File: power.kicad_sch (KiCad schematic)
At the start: 169 parts, among them Q10 SI7613DN-T1-GE3, Q2 BC817-25W, Q3 DZDH0401DW, Q4 DZDH0401DW, Q5 SI7613DN-T1-GE3, Q6 SI7613DN-T1-GE3, Q8 BC817-25W, U1 LT8350RV#PBF, U10 LM3881MME_NOPB, U11 AP22615A_TSOT26, U2 MP2386GG, U3 TPS65983BAZBHR, U9 LM1117MP-3.3_NOPB

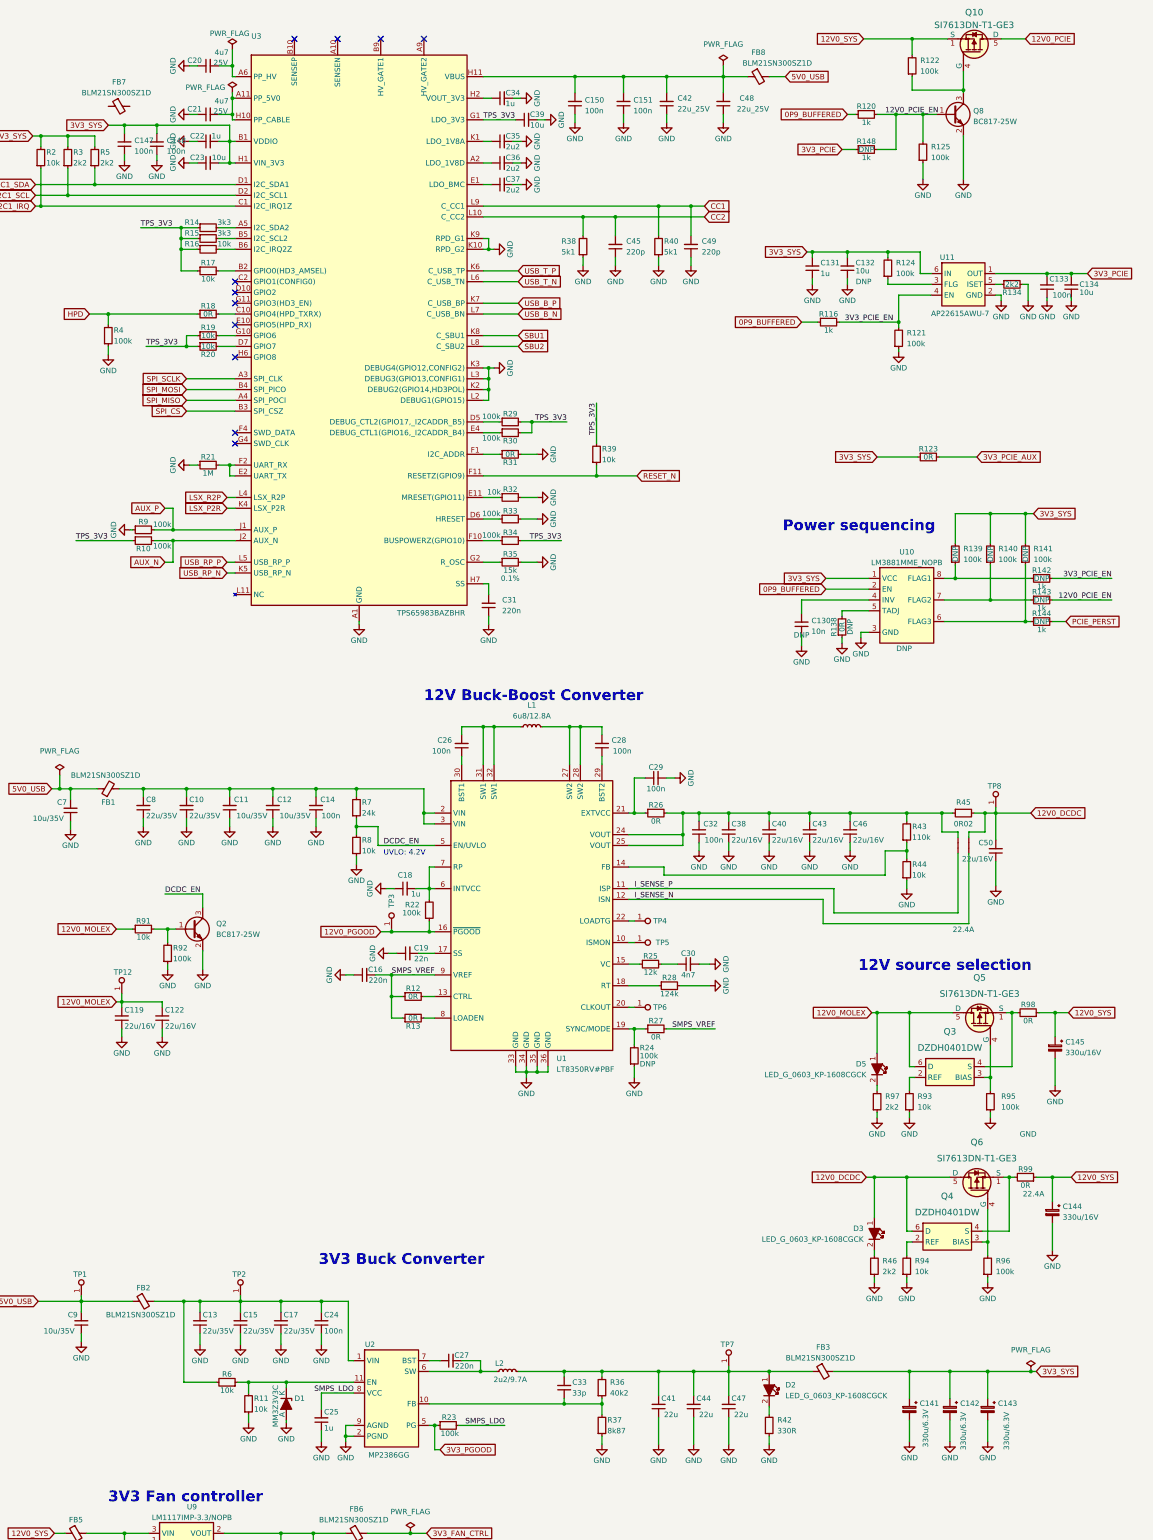
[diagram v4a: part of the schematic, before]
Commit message: Added DNP capacitors in empty spaces
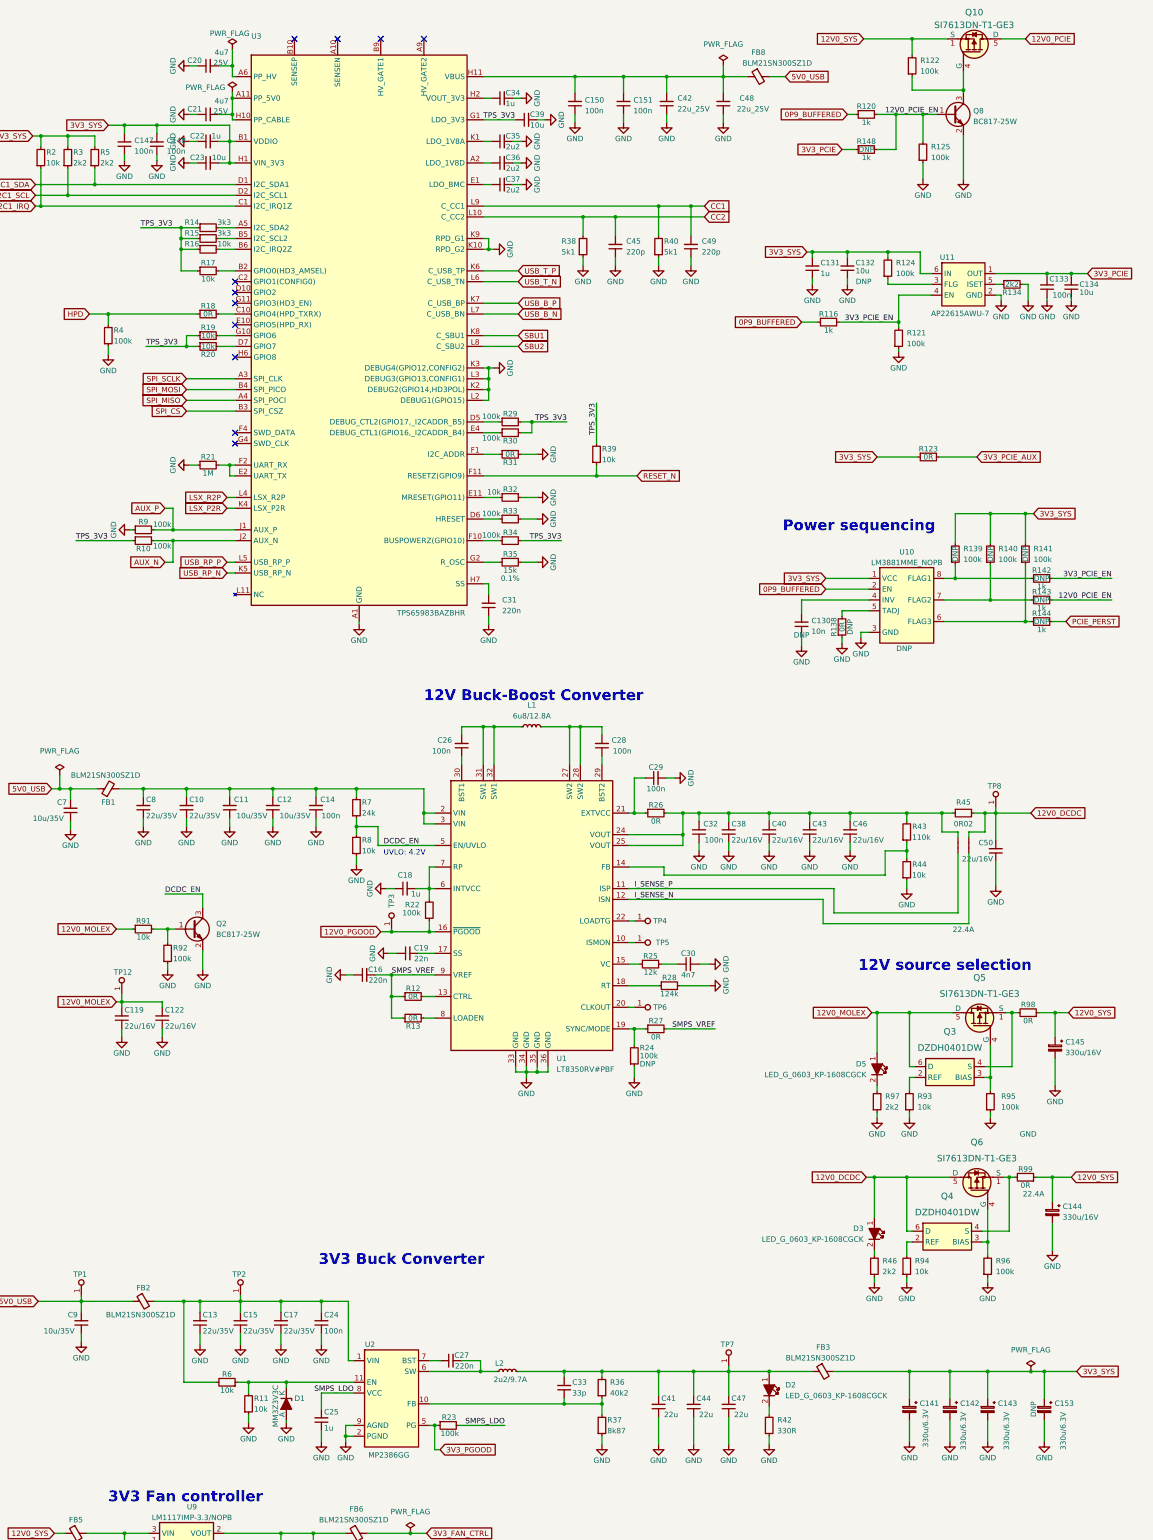
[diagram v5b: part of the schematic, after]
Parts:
- removed FB7: BLM21SN300SZ1D, thunderbolt-gpu-adapter-footprints:FB_0805_2012Metric, symbol thunderbolt-gpu-adapter:BLM21SN300SZ1D
- added C153: C_Pol_330u_6.3V_KEMET-T520-B, antmicro-footprints:C_Pol_EIA-B, symbol antmicroCapacitorspol:C_Pol_330u_6.3V_KEMET-T520-B
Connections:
- net 3V3_SYS: now also C153.1
- net GND: now also C153.2
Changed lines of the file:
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@@
   (junction (at 189.23 215.265) (diameter 0) (color 0 0 0 0)
   )
+  (junction (at 263.525 346.71) (diameter 0) (color 0 0 0 0)
+  )
   (junction (at 71.755 209.55) (diameter 0) (color 0 0 0 0)
   )
@@
     (stroke (width 0) (type default) (color 0 0 0 0))
   )
+  (wire (pts (xy 263.525 346.71) (xy 271.145 346.71))
+    (stroke (width 0) (type default) (color 0 0 0 0))
+  )
   (wire (pts (xy 45.085 242.57) (xy 48.895 242.57))
     (stroke (width 0) (type default) (color 0 0 0 0))
@@
     (stroke (width 0) (type default) (color 0 0 0 0))
   )
+  (wire (pts (xy 263.525 346.71) (xy 263.525 353.06))
+    (stroke (width 0) (type default) (color 0 0 0 0))
+  )
   (wire (pts (xy 51.435 216.535) (xy 51.435 218.44))
     (stroke (width 0) (type default) (color 0 0 0 0))
@@
     (stroke (width 0) (type default) (color 0 0 0 0))
   )
+  (wire (pts (xy 263.525 358.14) (xy 263.525 363.22))
+    (stroke (width 0) (type default) (color 0 0 0 0))
+  )
   (wire (pts (xy 46.355 259.715) (xy 55.88 259.715))
     (stroke (width 0) (type default) (color 0 0 0 0))
@@
     (stroke (width 0) (type default) (color 0 0 0 0))
   )
-  (wire (pts (xy 260.35 346.71) (xy 261.62 346.71))
+  (wire (pts (xy 260.35 346.71) (xy 263.525 346.71))
     (stroke (width 0) (type default) (color 0 0 0 0))
   )
@@
     )
   )
-  (global_label "3V3_SYS" (shape input) (at 261.62 346.71 0) (fields_autoplaced)
+  (global_label "3V3_SYS" (shape input) (at 271.145 346.71 0) (fields_autoplaced)
     (effects (font (size 1.27 1.27)) (justify left))
-    (property "Intersheet References" "${INTERSHEET_REFS}" (id 0) (at 272.016 346.6306 0)
+    (property "Intersheet References" "${INTERSHEET_REFS}" (id 0) (at 281.541 346.6306 0)
       (effects (font (size 1.27 1.27)) (justify left) hide)
     )
@@
     (pin "2")
   )
+  (symbol (lib_id "thunderbolt-gpu-adapter:GND") (at 263.525 363.22 0) (unit 1)
+    (in_bom yes) (on_board yes)
+    (property "Reference" "#PWR0226" (id 0) (at 263.525 369.57 0)
+      (effects (font (size 1.27 1.27)) hide)
+    )
+    (property "Value" "GND" (id 1) (at 263.525 367.03 0))
+    (property "Footprint" "" (id 2) (at 263.525 363.22 0)
+      (effects (font (size 1.27 1.27)) hide)
+    )
+    (property "Datasheet" "" (id 3) (at 263.525 363.22 0)
+      (effects (font (size 1.27 1.27)) hide)
+    )
+    (property "Author" "Antmicro" (id 4) (at 272.415 370.84 0)
+      (effects (font (size 1.27 1.27) (thickness 0.15)) (justify left bottom) hide)
+    )
+    (property "License" "Apache-2.0" (id 5) (at 272.415 373.38 0)
+      (effects (font (size 1.27 1.27) (thickness 0.15)) (justify left bottom) hide)
+    )
+    (pin "1")
+  )
   (symbol (lib_id "thunderbolt-gpu-adapter:C_10n_0402") (at 206.375 173.355 90) (unit 1)
     (in_bom yes) (on_board yes) (fields_autoplaced)
@@
     (pin "2")
   )
+  (symbol (lib_id "antmicroCapacitorspol:C_Pol_330u_6.3V_KEMET-T520-B") (at 263.525 353.06 270) (unit 1)
+    (in_bom yes) (on_board yes)
+    (property "Reference" "C153" (id 0) (at 265.938 354.236 90)
+      (effects (font (size 1.27 1.27) (thickness 0.15)) (justify left))
+    )
+    (property "Value" "C_Pol_330u_6.3V_KEMET-T520-B" (id 1) (at 260.985 367.03 0)
+      (effects (font (size 1.27 1.27) (thickness 0.15)) (justify left bottom) hide)
+    )
+    (property "Footprint" "antmicro-footprints:C_Pol_EIA-B" (id 2) (at 255.905 367.03 0)
+      (effects (font (size 1.27 1.27) (thickness 0.15)) (justify left bottom) hide)
+    )
+    (property "Datasheet" "https://content.kemet.com/datasheets/KEM_T2076_T52X-530.pdf" (id 3) (at 253.365 367.03 0)
+      (effects (font (size 1.27 1.27) (thickness 0.15)) (justify left bottom) hide)
+    )
+    (property "Val" "330u/6.3V" (id 4) (at 267.97 356.235 0)
+      (effects (font (size 1.27 1.27) (thickness 0.15)) (justify left))
+    )
+    (property "MPN" "T520B337M006ATE040" (id 5) (at 250.825 367.03 0)
+      (effects (font (size 1.27 1.27) (thickness 0.15)) (justify left bottom) hide)
+    )
+    (property "Manufacturer" "KEMET" (id 6) (at 248.285 367.03 0)
+      (effects (font (size 1.27 1.27) (thickness 0.15)) (justify left bottom) hide)
+    )
+    (property "License" "Apache-2.0" (id 7) (at 245.745 367.03 0)
+      (effects (font (size 1.27 1.27) (thickness 0.15)) (justify left bottom) hide)
+    )
+    (property "Author" "Antmicro" (id 8) (at 243.205 367.03 0)
+      (effects (font (size 1.27 1.27) (thickness 0.15)) (justify left bottom) hide)
+    )
+    (property "Voltage" "6.3V" (id 9) (at 240.665 367.03 0)
+      (effects (font (size 1.27 1.27)) (justify left bottom) hide)
+    )
+    (property "Dielectric" "template_dielectric" (id 10) (at 238.125 367.03 0)
+      (effects (font (size 1.27 1.27)) (justify left bottom) hide)
+    )
+    (property "DNP" "DNP" (id 11) (at 260.985 355.6 0))
+    (pin "1")
+    (pin "2")
+  )
   (symbol (lib_id "thunderbolt-gpu-adapter:R_8k87_0402") (at 159.385 361.95 90) (unit 1)
     (in_bom yes) (on_board yes)
@@
       (effects (font (size 1.27 1.27) (thickness 0.15)) (justify left bottom) hide)
     )
-    (pin "1")
-    (pin "2")
-  )
-  (symbol (lib_id "thunderbolt-gpu-adapter:BLM21SN300SZ1D") (at 43.18 48.895 0) (mirror x) (unit 1)
-    (in_bom yes) (on_board yes)
-    (property "Reference" "FB7" (id 0) (at 45.72 43.18 0)
-      (effects (font (size 1.27 1.27) (thickness 0.15)))
-    )
-    (property "Value" "BLM21SN300SZ1D" (id 1) (at 45.085 45.72 0)
-      (effects (font (size 1.27 1.27) (thickness 0.15)))
-    )
-    (property "Footprint" "thunderbolt-gpu-adapter-footprints:FB_0805_2012Metric" (id 2) (at 57.15 43.815 0)
-      (effects (font (size 1.27 1.27) (thickness 0.15)) (justify left bottom) hide)
-    )
-    (property "Datasheet" "https://www.murata.com/en-sg/products/productdata/8796738977822/ENFA0005.pdf?1519270210000" (id 3) (at 57.15 41.275 0)
-      (effects (font (size 1.27 1.27) (thickness 0.15)) (justify left bottom) hide)
-    )
-    (property "MPN" "BLM21SN300SZ1D" (id 4) (at 57.15 38.735 0)
-      (effects (font (size 1.27 1.27) (thickness 0.15)) (justify left bottom) hide)
-    )
-    (property "Manufacturer" "Murata" (id 5) (at 57.15 36.195 0)
-      (effects (font (size 1.27 1.27) (thickness 0.15)) (justify left bottom) hide)
-    )
-    (property "License" "Apache-2.0" (id 7) (at 57.15 31.115 0)
-      (effects (font (size 1.27 1.27) (thickness 0.15)) (justify left bottom) hide)
-    )
-    (property "Author" "Antmicro" (id 8) (at 57.15 33.655 0)
-      (effects (font (size 1.27 1.27) (thickness 0.15)) (justify left bottom) hide)
-    )

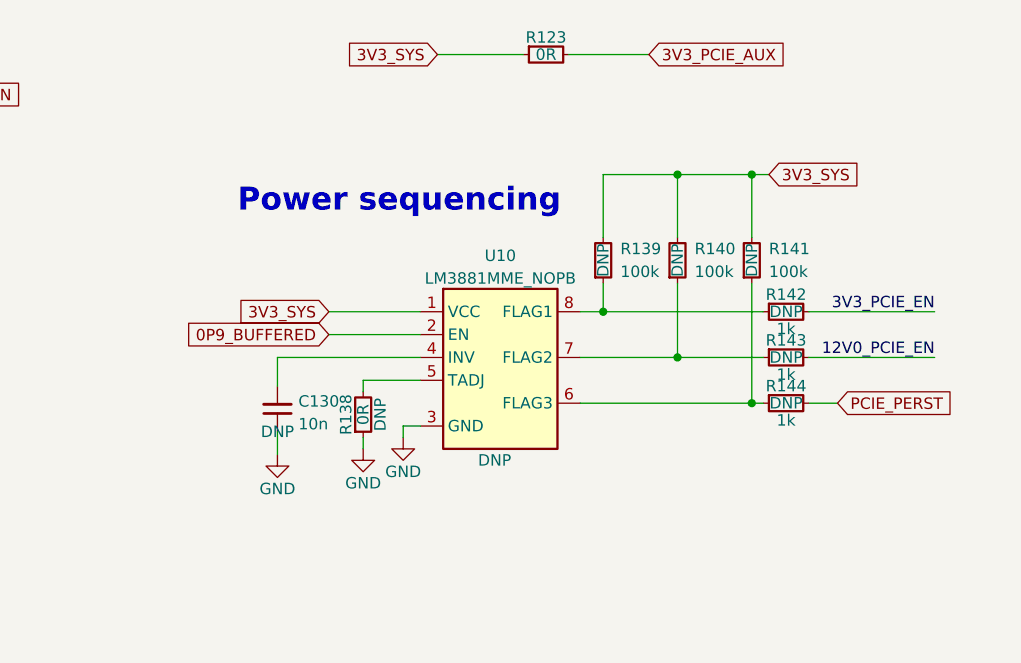
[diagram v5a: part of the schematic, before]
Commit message: Removed optional power sequencing
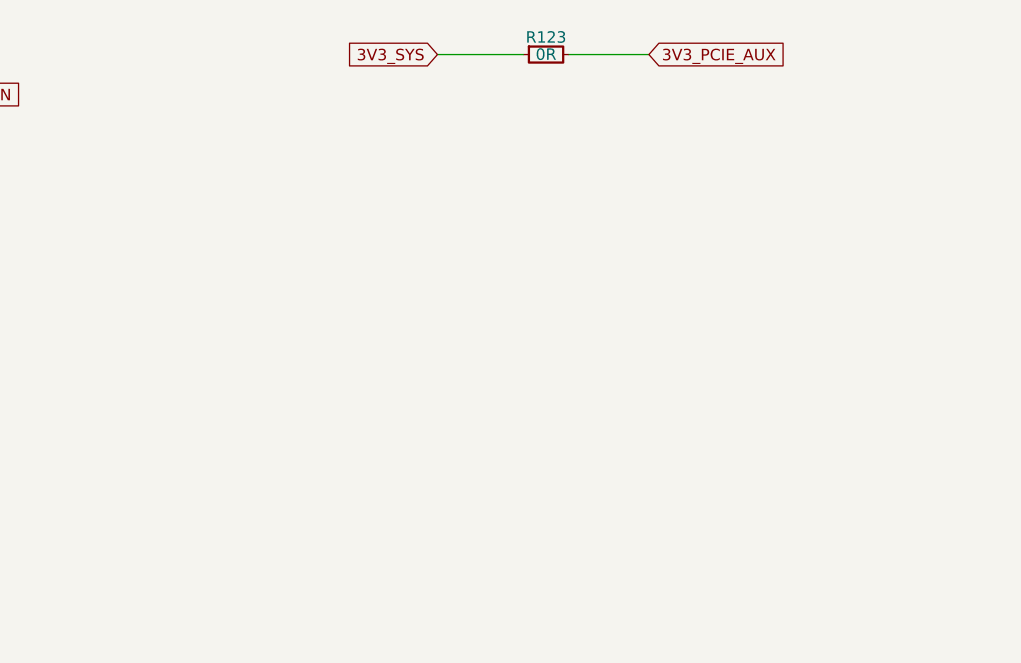
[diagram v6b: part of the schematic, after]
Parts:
- removed C130: C_10n_0402, thunderbolt-gpu-adapter-footprints:C_0402_1005Metric, symbol thunderbolt-gpu-adapter:C_10n_0402
- removed R138: R_0R_0402, thunderbolt-gpu-adapter-footprints:R_0402_1005Metric, symbol thunderbolt-gpu-adapter:R_0R_0402
- removed R139, R140, R141: R_100k_0402, thunderbolt-gpu-adapter-footprints:R_0402_1005Metric, symbol thunderbolt-gpu-adapter:R_100k_0402
- removed R142, R143, R144: R_1k_0402, thunderbolt-gpu-adapter-footprints:R_0402_1005Metric, symbol thunderbolt-gpu-adapter:R_1k_0402
- removed U10: LM3881MME_NOPB, thunderbolt-gpu-adapter-footprints:VSSOP-8_3x3mm_P0.65mm, symbol thunderbolt-gpu-adapter:LM3881MME_NOPB
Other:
- note removed: "Power sequencing"
